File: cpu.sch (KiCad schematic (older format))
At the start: 22 parts, among them SW1 RESET, U1 Z80CPU, U2 74HC04, Y1 7.3728MHz

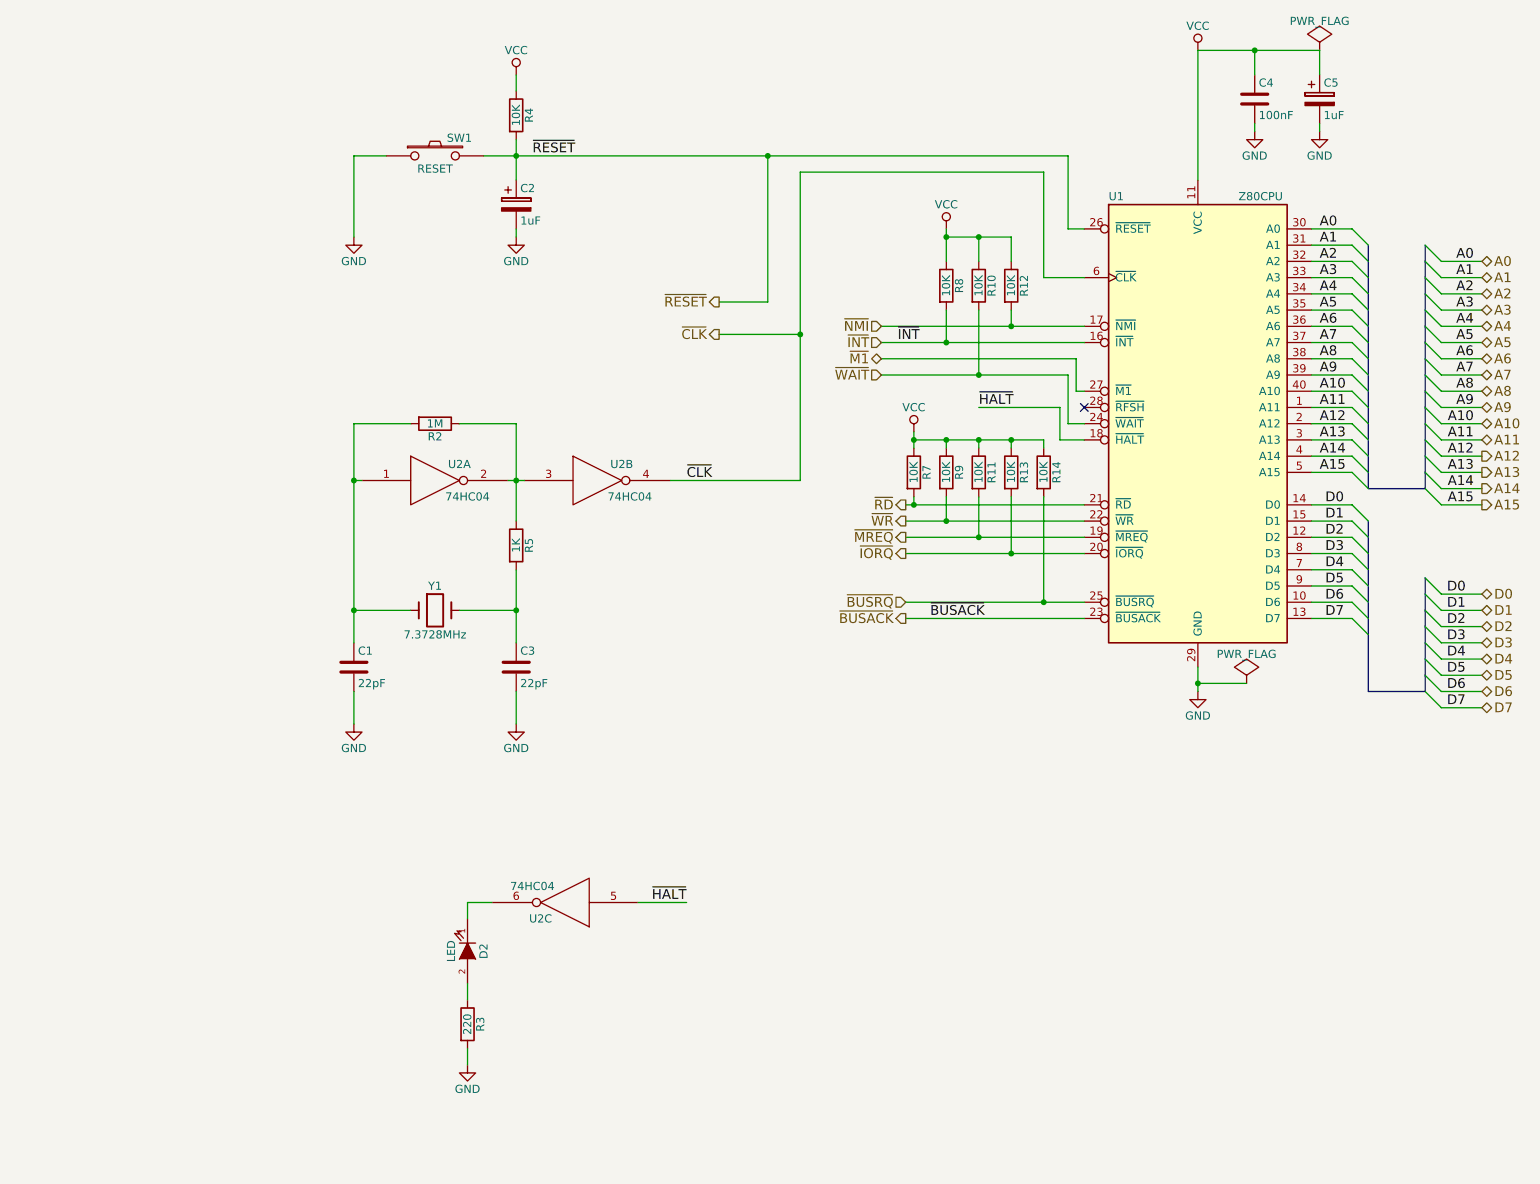
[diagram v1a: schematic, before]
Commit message: Added basic board layout WIP
Switched a few bus lines around to make the layout a little easier.
Still learning PCBNew, has a few quirks I haven't figured out yet.
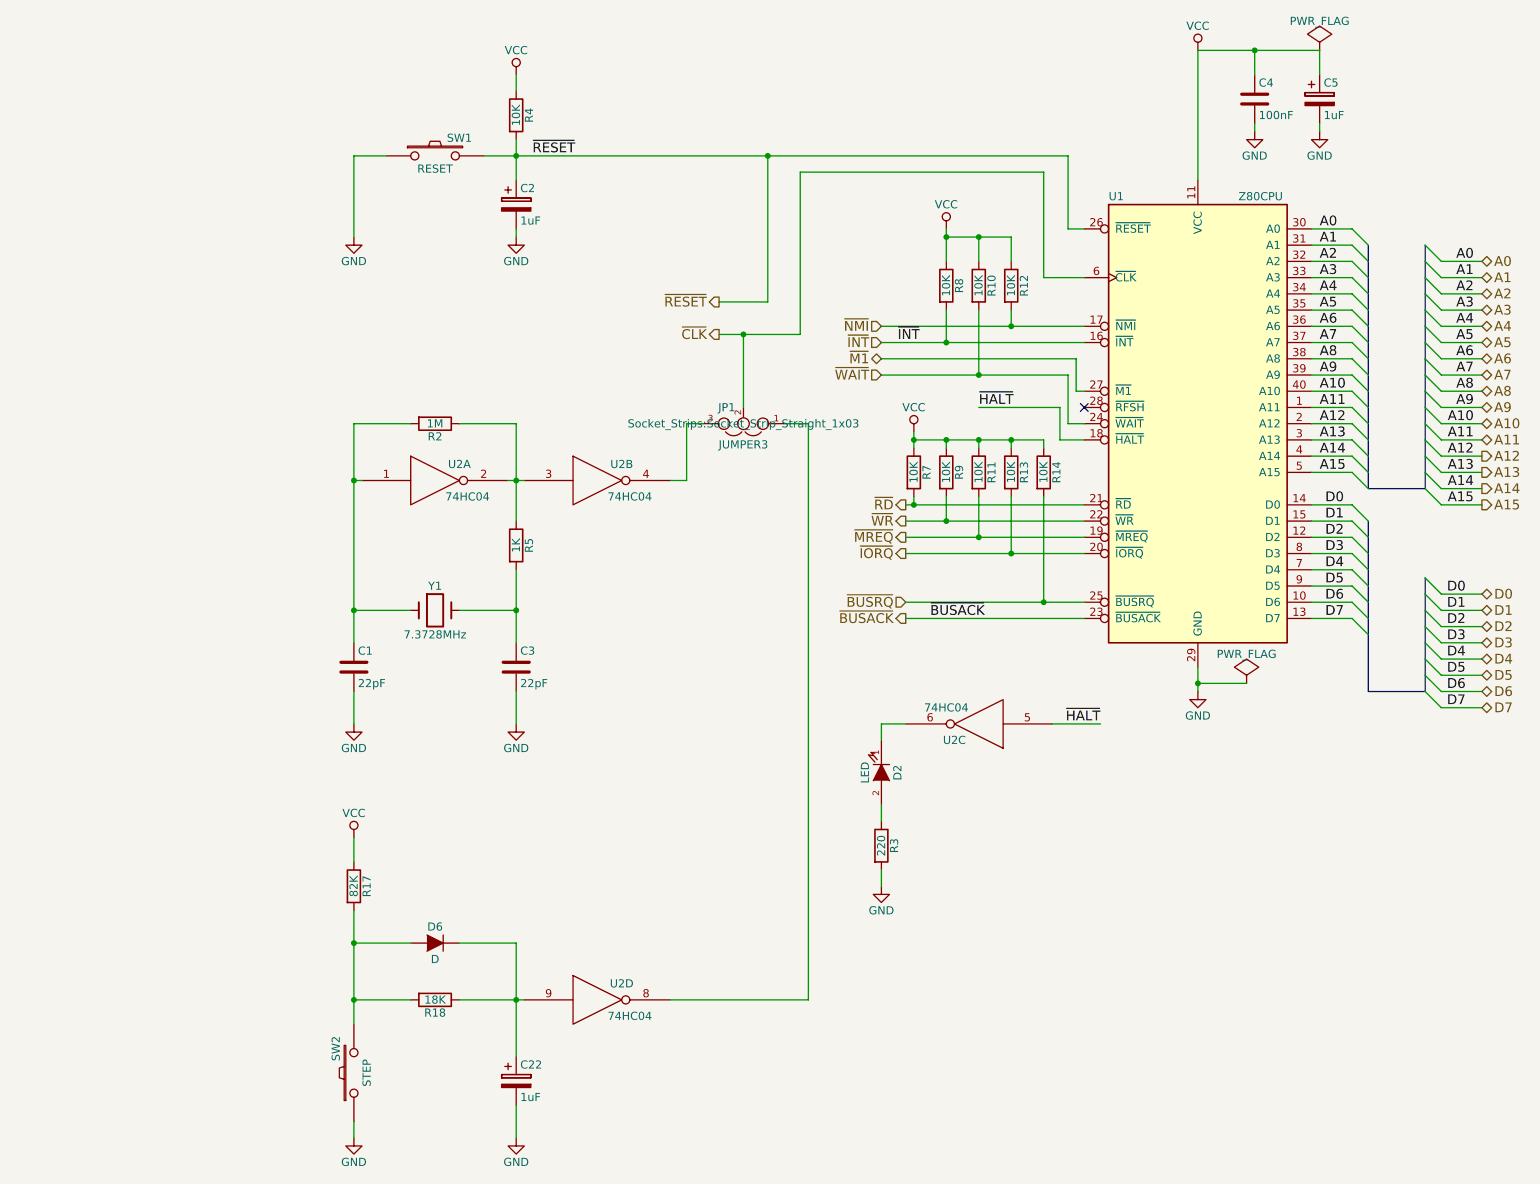
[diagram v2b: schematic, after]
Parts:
- added C22: 1uF, Capacitors_SMD:c_elec_4x4.5, symbol CP
- added D6: D, Diodes_SMD:MiniMELF_Standard, symbol D
- added JP1: JUMPER3, Socket_Strips:Socket_Strip_Straight_1x03, symbol JUMPER3
- added R17: 82K, Resistors_SMD:R_0805_HandSoldering, symbol R
- added R18: 18K, Resistors_SMD:R_0805_HandSoldering, symbol R
- added SW2: STEP, Buttons_Switches_SMD:SW_SPST_B3SL-1002P, symbol SW_PUSH
- added unit 4 of U2
- C2, C5: footprint Capacitors_ThroughHole:C_Radial_D6.3_L11.2_P2.5 -> Capacitors_SMD:c_elec_4x4.5
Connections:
- net GND: now also C22.2, SW2.1, U2.7 (GND)
- net VCC: now also R17.1, U2.14 (VCC)
- net ~CLK: now also JP1.2; no longer U2.4
- new net: JP1.3, U2.4
- new net: JP1.1, U2.8
- new net: C22.1, D6.1 (K), R18.1, U2.9
- new net: D6.2 (A), R17.2, R18.2, SW2.2
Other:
- moved on the sheet: D2, R3, U2C
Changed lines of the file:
@@
 Text Label 4150 1400 0    60   ~ 0
 ~RESET
-Text Label 5100 3400 0    60   ~ 0
-~CLK
 Wire Wire Line
 	7400 3150 7400 2950
@@
 	1    0    0    -1
 $EndComp
-Wire Wire Line
-	5800 3400 5000 3400
-Wire Wire Line
-	5800 1500 5800 3400
 $Comp
 L 74HC04 U2
@@
 L 74HC04 U2
 U 3 1 577B33CF
-P 4350 6000
-F 0 "U2" H 4500 6100 50  0000 C CNN
-F 1 "74HC04" H 4550 5900 50  0000 C CNN
-F 2 "Housings_DIP:DIP-14_W7.62mm_LongPads" H 4350 6000 50  0001 C CNN
-F 3 "" H 4350 6000 50  0000 C CNN
-	3    4350 6000
+P 6900 4900
+F 0 "U2" H 7050 5000 50  0000 C CNN
+F 1 "74HC04" H 7100 4800 50  0000 C CNN
+F 2 "Housings_DIP:DIP-14_W7.62mm_LongPads" H 6900 4900 50  0001 C CNN
+F 3 "" H 6900 4900 50  0000 C CNN
+	3    6900 4900
 	-1   0    0    1
 $EndComp
 Wire Wire Line
-	4800 6000 5100 6000
-Text Label 5100 6000 2    60   ~ 0
+	7350 4900 7650 4900
+Text Label 7650 4900 2    60   ~ 0
 ~HALT
 $Comp
 L LED D2
 U 1 1 577B3772
-P 3750 6300
-F 0 "D2" H 3750 6400 50  0000 C CNN
-F 1 "LED" H 3750 6200 50  0000 C CNN
-F 2 "LEDs:LED-3MM" H 3750 6300 50  0001 C CNN
-F 3 "" H 3750 6300 50  0000 C CNN
-	1    3750 6300
+P 6300 5200
+F 0 "D2" H 6300 5300 50  0000 C CNN
+F 1 "LED" H 6300 5100 50  0000 C CNN
+F 2 "LEDs:LED-3MM" H 6300 5200 50  0001 C CNN
+F 3 "" H 6300 5200 50  0000 C CNN
+	1    6300 5200
 	0    1    1    0
 $EndComp
@@
 L R R3
 U 1 1 577B3778
-P 3750 6750
-F 0 "R3" V 3830 6750 50  0000 C CNN
-F 1 "220" V 3750 6750 50  0000 C CNN
-F 2 "Resistors_SMD:R_0805_HandSoldering" V 3680 6750 50  0001 C CNN
-F 3 "" H 3750 6750 50  0000 C CNN
-	1    3750 6750
+P 6300 5650
+F 0 "R3" V 6380 5650 50  0000 C CNN
+F 1 "220" V 6300 5650 50  0000 C CNN
+F 2 "Resistors_SMD:R_0805_HandSoldering" V 6230 5650 50  0001 C CNN
+F 3 "" H 6300 5650 50  0000 C CNN
+	1    6300 5650
 	1    0    0    -1
 $EndComp
@@
 L GND #PWR07
 U 1 1 577B377E
-P 3750 7000
-F 0 "#PWR07" H 3750 6750 50  0001 C CNN
-F 1 "GND" H 3750 6850 50  0000 C CNN
-F 2 "" H 3750 7000 50  0000 C CNN
-F 3 "" H 3750 7000 50  0000 C CNN
-	1    3750 7000
-	1    0    0    -1
-$EndComp
-Wire Wire Line
-	3750 6500 3750 6600
-Wire Wire Line
-	3750 6900 3750 7000
-Wire Wire Line
-	3750 6100 3750 6000
-Wire Wire Line
-	3750 6000 3900 6000
+P 6300 5900
+F 0 "#PWR07" H 6300 5650 50  0001 C CNN
+F 1 "GND" H 6300 5750 50  0000 C CNN
+F 2 "" H 6300 5900 50  0000 C CNN
+F 3 "" H 6300 5900 50  0000 C CNN
+	1    6300 5900
+	1    0    0    -1
+$EndComp
+Wire Wire Line
+	6300 5400 6300 5500
+Wire Wire Line
+	6300 5800 6300 5900
+Wire Wire Line
+	6300 5000 6300 4900
+Wire Wire Line
+	6300 4900 6450 4900
 Wire Wire Line
 	3250 1400 3050 1400
@@
 F 0 "C2" H 4075 1800 50  0000 L CNN
 F 1 "1uF" H 4075 1600 50  0000 L CNN
-F 2 "Capacitors_ThroughHole:C_Radial_D6.3_L11.2_P2.5" H 4088 1550 50  0001 C CNN
+F 2 "Capacitors_SMD:c_elec_4x4.5" H 4088 1550 50  0001 C CNN
 F 3 "" H 4050 1700 50  0000 C CNN
 	1    4050 1700
@@
 F 0 "C5" H 9025 1150 50  0000 L CNN
 F 1 "1uF" H 9025 950 50  0000 L CNN
-F 2 "Capacitors_ThroughHole:C_Radial_D6.3_L11.2_P2.5" H 9038 900 50  0001 C CNN
+F 2 "Capacitors_SMD:c_elec_4x4.5" H 9038 900 50  0001 C CNN
 F 3 "" H 9000 1050 50  0000 C CNN
 	1    9000 1050
@@
 $EndComp
 Wire Wire Line
-	9000 900  9000 750
-Wire Wire Line
-	9000 750  8250 750
+	9000 750  9000 900
+Wire Wire Line
+	8250 750  9000 750
 Wire Wire Line
 	8600 900  8600 750
@@
 Wire Wire Line
 	9000 1200 9000 1250
-Wire Wire Line
-	5800 2500 5300 2500
-Connection ~ 5800 2500
 Text HLabel 5300 2500 0    60   Output ~ 0
 ~CLK
@@
 Text HLabel 6300 2450 0    60   Input ~ 0
 ~NMI
+Wire Wire Line
+	5300 2500 5800 2500
+Wire Wire Line
+	5800 2500 5800 1500
+$Comp
+L JUMPER3 JP1
+U 1 1 578B8AE0
+P 5450 3050
+F 0 "JP1" H 5500 2950 50  0000 L CNN
+F 1 "JUMPER3" H 5450 3150 50  0000 C BNN
+F 2 "Socket_Strips:Socket_Strip_Straight_1x03" H 5450 3050 50  0000 C CNN
+F 3 "" H 5450 3050 50  0000 C CNN
+	1    5450 3050
+	-1   0    0    1
+$EndComp
+Wire Wire Line
+	5000 3400 5100 3400
+Wire Wire Line
+	5100 3400 5100 3050
+Wire Wire Line
+	5100 3050 5200 3050
+Wire Wire Line
+	5450 2950 5450 2500
+Connection ~ 5450 2500
+Wire Wire Line
+	5700 3050 5850 3050
+Wire Wire Line
+	5850 3050 5850 6600
+Wire Wire Line
+	5850 6600 5000 6600
+$Comp
+L 74HC04 U2
+U 4 1 578B911B
+P 4550 6600
+F 0 "U2" H 4700 6700 50  0000 C CNN
+F 1 "74HC04" H 4750 6500 50  0000 C CNN
+F 2 "Housings_DIP:DIP-14_W7.62mm_LongPads" H 4550 6600 50  0001 C CNN
+F 3 "" H 4550 6600 50  0000 C CNN
+	4    4550 6600
+	1    0    0    -1
+$EndComp
+$Comp
+L CP C22
+U 1 1 578B92CB
+P 4050 7100
+F 0 "C22" H 4075 7200 50  0000 L CNN
+F 1 "1uF" H 4075 7000 50  0000 L CNN
+F 2 "Capacitors_SMD:c_elec_4x4.5" H 4088 6950 50  0001 C CNN
+F 3 "" H 4050 7100 50  0000 C CNN
+	1    4050 7100
+	1    0    0    -1
+$EndComp
+Wire Wire Line
+	4050 6250 4050 6950
+Wire Wire Line
+	3700 6600 4100 6600
+$Comp
+L R R18
+U 1 1 578B9404
+P 3550 6600
+F 0 "R18" V 3630 6600 50  0000 C CNN
+F 1 "18K" V 3550 6600 50  0000 C CNN
+F 2 "Resistors_SMD:R_0805_HandSoldering" V 3480 6600 50  0001 C CNN
+F 3 "" H 3550 6600 50  0000 C CNN
+	1    3550 6600
+	0    1    1    0
+$EndComp
+Connection ~ 4050 6600
+$Comp
+L R R17
+U 1 1 578B957E
+P 3050 5900
+F 0 "R17" V 3130 5900 50  0000 C CNN
+F 1 "82K" V 3050 5900 50  0000 C CNN
+F 2 "Resistors_SMD:R_0805_HandSoldering" V 2980 5900 50  0001 C CNN
+F 3 "" H 3050 5900 50  0000 C CNN
+	1    3050 5900
+	1    0    0    -1
+$EndComp
+Wire Wire Line
+	3050 6050 3050 6750
+Wire Wire Line
+	3050 6600 3400 6600
+$Comp
+L VCC #PWR015
+U 1 1 578B96BA
+P 3050 5600
+F 0 "#PWR015" H 3050 5450 50  0001 C CNN
+F 1 "VCC" H 3050 5750 50  0000 C CNN
+F 2 "" H 3050 5600 50  0000 C CNN
+F 3 "" H 3050 5600 50  0000 C CNN
+	1    3050 5600
+	1    0    0    -1
+$EndComp
+Wire Wire Line
+	3050 5600 3050 5750
+$Comp
+L D D6
+U 1 1 578B9985
+P 3550 6250
+F 0 "D6" H 3550 6350 50  0000 C CNN
+F 1 "D" H 3550 6150 50  0000 C CNN
+F 2 "Diodes_SMD:MiniMELF_Standard" H 3550 6250 50  0001 C CNN
+F 3 "" H 3550 6250 50  0000 C CNN
+	1    3550 6250
+	-1   0    0    -1
+$EndComp
+Wire Wire Line
+	3400 6250 3050 6250
+Connection ~ 3050 6250
+Wire Wire Line
+	3700 6250 4050 6250
+$Comp
+L SW_PUSH SW2
+U 1 1 578B9BE1
+P 3050 7050
+F 0 "SW2" H 3200 7160 50  0000 C CNN
+F 1 "STEP" H 3050 6970 50  0000 C CNN
+F 2 "Buttons_Switches_SMD:SW_SPST_B3SL-1002P" H 3050 7050 50  0001 C CNN
+F 3 "" H 3050 7050 50  0000 C CNN
+	1    3050 7050
+	0    -1   -1   0
+$EndComp
+Connection ~ 3050 6600
+$Comp
+L GND #PWR016
+U 1 1 578B9D53
+P 3050 7450
+F 0 "#PWR016" H 3050 7200 50  0001 C CNN
+F 1 "GND" H 3050 7300 50  0000 C CNN
+F 2 "" H 3050 7450 50  0000 C CNN
+F 3 "" H 3050 7450 50  0000 C CNN
+	1    3050 7450
+	1    0    0    -1
+$EndComp
+$Comp
+L GND #PWR017
+U 1 1 578B9DBB
+P 4050 7450
+F 0 "#PWR017" H 4050 7200 50  0001 C CNN
+F 1 "GND" H 4050 7300 50  0000 C CNN
+F 2 "" H 4050 7450 50  0000 C CNN
+F 3 "" H 4050 7450 50  0000 C CNN
+	1    4050 7450
+	1    0    0    -1
+$EndComp
+Wire Wire Line
+	4050 7450 4050 7250
+Wire Wire Line
+	3050 7450 3050 7350
 $EndSCHEMATC

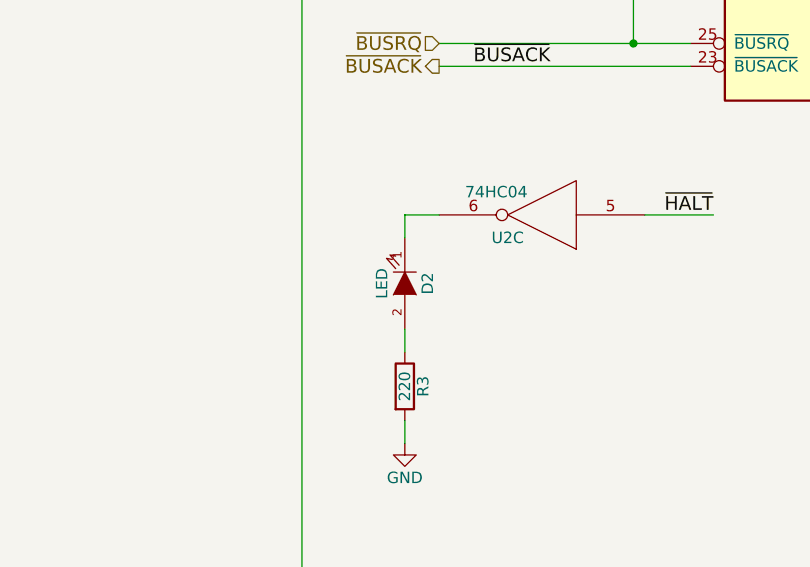
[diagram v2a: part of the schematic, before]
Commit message: Updated LEDs, added power supply options, added mounting holes in schematic.
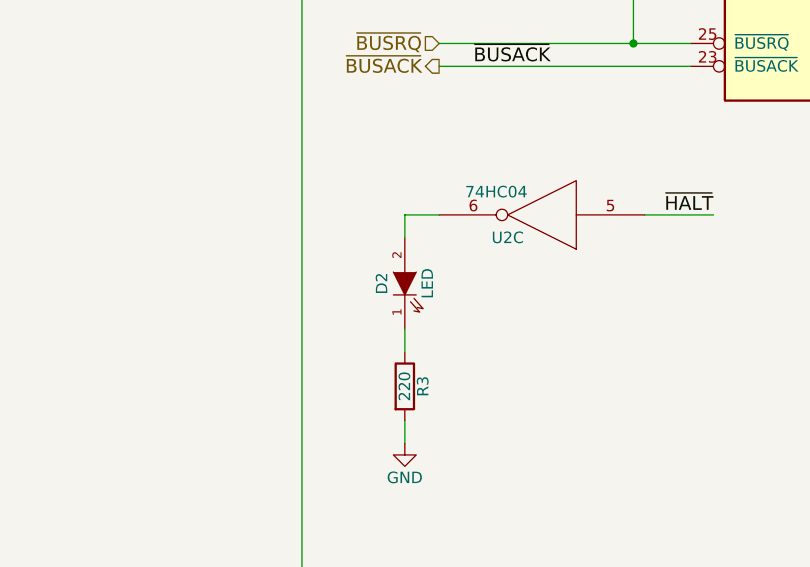
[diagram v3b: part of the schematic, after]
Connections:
- net at U2.6: now also D2.2 (A); no longer D2.1 (K)
- net at R3.1: now also D2.1 (K); no longer D2.2 (A)
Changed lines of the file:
@@
 LIBS:microchip_pic18mcu
 LIBS:6850
+LIBS:nrc2016
 LIBS:z80-cache
 EELAYER 25 0
@@
 F 3 "" H 6300 5200 50  0000 C CNN
 	1    6300 5200
-	0    1    1    0
-$EndComp
-$Comp
+	0    -1   -1   0
+$EndComp
+$Comp
